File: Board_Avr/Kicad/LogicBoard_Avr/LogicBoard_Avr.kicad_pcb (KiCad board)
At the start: 4 copper layers, 89.2 x 87.8 mm, 56 parts, among them J1 I2C_Interface, J10 PSU Connector, J11 TriggeredStatusLedConnector, J12 PowerStatusLedConnector, J2 UART_Interface, J3 Mechanical user interface mai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, J4 Power board connector, J5 SPI Connector, J6 ICSP Header, J9 GPIO Connector, SW1 Reset switch, U1 ATmega328PB-A, U2 TLP291, U3 TLV1117-33IDCYRG3, U4 LM1117-5.0, X1 ASV-12.000MHZ-EJ-T, Y1 ABLS-20.000MHz-16-A-4-H-T

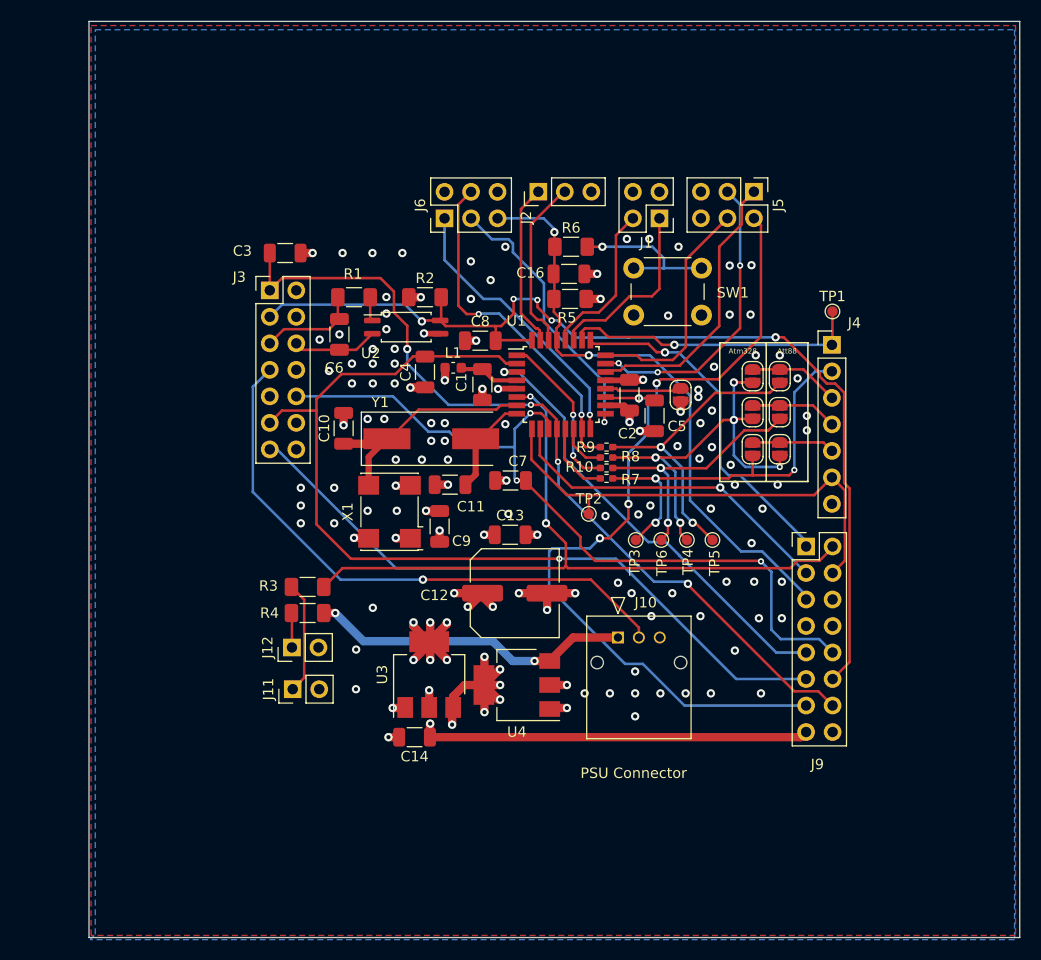
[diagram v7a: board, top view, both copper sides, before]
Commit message: Tweaked top silkscreen to embed useful information
Signed-off-by: bebenlebricolo <benoittarrade@hotmail.fr>
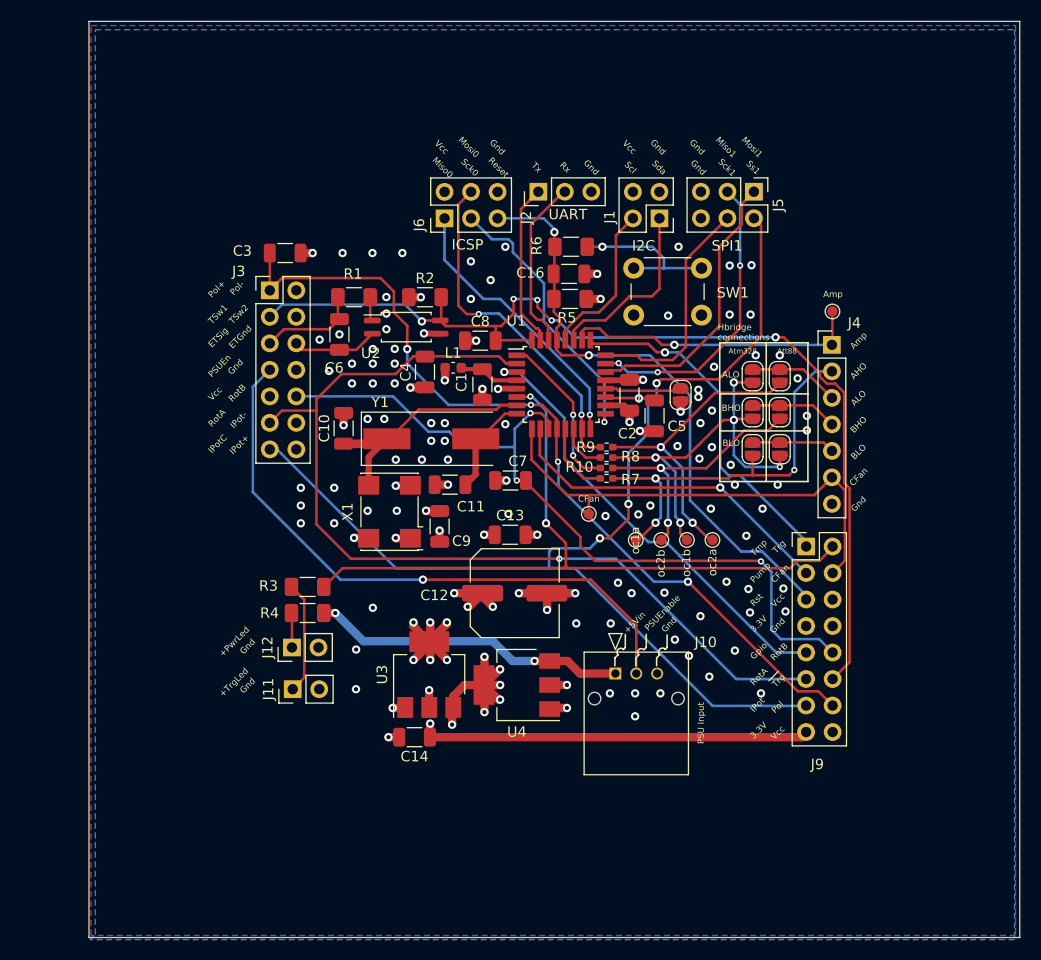
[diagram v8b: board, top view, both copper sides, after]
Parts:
- moved J10 3.46 mm to (155.2, 117.7)
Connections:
- net Net-(J11-Pad1) renamed /+TriggeredStatusLed
- net Net-(J12-Pad1) renamed /PowerRegulation/+PowerStatusLed
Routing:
- net /PSU_Enabled: track 55.7 -> 59.1 mm
- net /IntensityPot(In): track 116.7 -> 115.6 mm
- net /5V_PSU: track 31.0 -> 30.4 mm
- net GND: vias 113 -> 111
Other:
- board text added: "+5Vin"
- board text added: "+PwrLed"
- board text added: "+TrgLed"
- board text added: "3.3V"
- board text added: "<- 3.3V and Vcc exposed"
- board text added: "<- 3.3V and Vcc rails exposed"
- board text added: "<- Additional GPIO and RotaryEncoderB pin for breakout"
- board text added: "<- Cooling fan drive signal"
- board text added: "<- Current shunt amperemeter measure line"
- board text added: "<- External pump drive signal and Cooling fan drive signal"
- board text added: "<- Ground for boards gnd sharing"
- board text added: "<- HBridge A High Output (top left mosfet)"
- board text added: "<- HBridge A Low Output (bottom left mosfet)"
- board text added: "<- HBridge B High Output (top right mosfet)"
- board text added: "<- HBridge B Low Output (bottom right mosfet)"
- board text added: "<- Intensity potentiometer ADC input exposed and Polarity input pin exposed"
- board text added: "<- Reset line exposed and Vcc"
- board text added: "<- RotaryEncoderA pin for breakout and Inverted triggered status signal (MCU input exposed)"
- board text added: "<- Temperature probe (0-5V analog) and Triggered status signal"
- board text added: "AHO"
- board text added: "ALO"
- board text added: "Amp"
- board text added: "BHO"
- board text added: "BLO"
- board text added: "CFan"
- board text added: "ETGnd"
- board text added: "ETSig"
- board text added: "External trigger optoisolator ->"
- board text added: "Gnd"
- board text added: "Gpio"
- board text added: "Hbridge connections"
- board text added: "I2C"
- board text added: "ICSP"
- board text added: "IPot"
- board text added: "IPot+"
- board text added: "IPot-"
- board text added: "IPotC"
- board text added: "Itensity potentiometer positive and cursor pins ->"
- board text added: "Miso0"
- board text added: "Miso1"
- board text added: "Mosi0"
- board text added: "Mosi1"
- board text added: "PSU Input"
- board text added: "PSU enable switch ->"
- board text added: "PSUEn"
- board text added: "PSUEnable"
- board text added: "Pol"
- board text added: "Pol+"
- board text added: "Pol-"
- board text added: "Polarity swich connects here ->"
- board text added: "Power status LED ->"
- board text added: "Pump"
- board text added: "Reset"
- board text added: "RotA"
- board text added: "RotB"
- board text added: "Rotary encoder Vcc and pin B ->"
- board text added: "Rotary encoder pin A and Intensity potentiometer negative reference ->"
- board text added: "Rst"
- board text added: "Rx"
- board text added: "SPI1"
- board text added: "Sck0"
- board text added: "Sck1"
- board text added: "Scl"
- board text added: "Sda"
- board text added: "Ss1"
- board text added: "TSw1"
- board text added: "TSw2"
- board text added: "Tmp"
- board text added: "Trg"
- board text added: "Trigger manual switch ->"
- board text added: "Triggered status LED ->"
- board text added: "Tx"
- board text added: "UART"
- board text added: "Vcc"
- board text added: "oc1a"
- board text added: "oc1b"
- board text added: "oc2a"
- board text added: "oc2b"
